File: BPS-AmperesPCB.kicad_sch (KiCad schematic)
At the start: 44 parts, among them J1 Conn_01x04, J2 PeripheralCANConnector, J3 PeripheralCANConnector, U1 PeripheralSOM, U2 INA145UA/2K5, U3 AMC1300BDWV, U4 RO-123.3S_HP

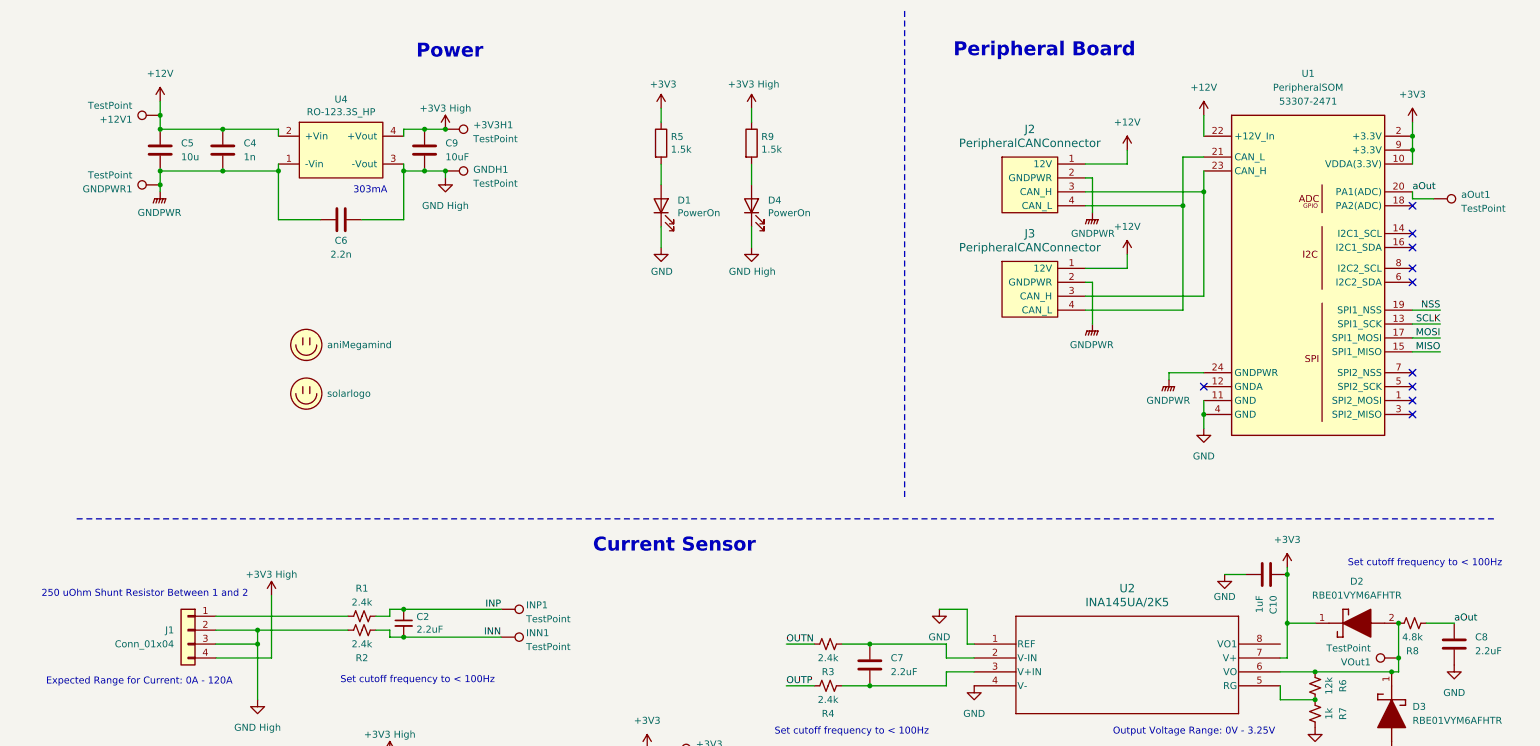
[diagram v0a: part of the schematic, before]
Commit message: initial sch change, added PSOM components
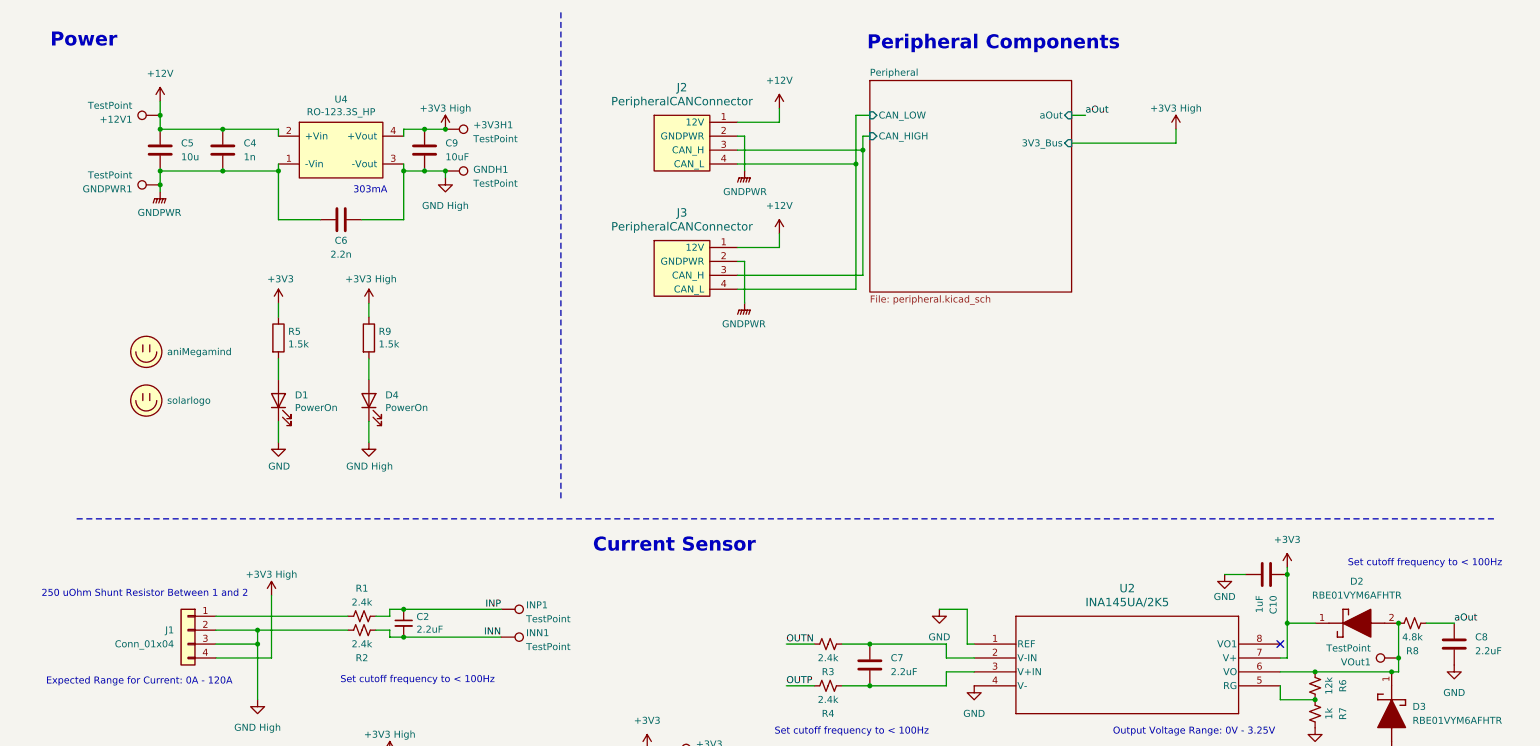
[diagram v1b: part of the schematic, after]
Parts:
- removed U1: PeripheralSOM, UTSVT_Special:PeripheralSOM, symbol utsvt-misc:PeripheralSOM
- removed aOut1: TestPoint, TestPoint:TestPoint_Keystone_5005-5009_Compact, symbol Connector:TestPoint
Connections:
- net Peripheral/CAN_HIGH: now reaches J2.3 (CAN_H), J3.3 (CAN_H)
- net Peripheral/CAN_LOW: now reaches J2.4 (CAN_L), J3.4 (CAN_L)
- no-connect marks 10 -> 1
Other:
- added sheet Peripheral (peripheral.kicad_sch)
- note added: "Peripheral Components"
- note removed: "Peripheral Board"
- moved on the sheet: D1, D4, R5, R9

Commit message: migrated to KiCad 9
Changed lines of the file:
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@@
 (kicad_sch
-	(version 20231120)
+	(version 20250114)
 	(generator "eeschema")
-	(generator_version "8.0")
+	(generator_version "9.0")
 	(paper "A4")
+	(text "Maximum Voltage Protected: -2.7V - 6V"
+		(exclude_from_sim no)
+		(at 261.366 158.75 0)
+		(effects
+			(font
+				(size 1.27 1.27)
+			)
+		)
+	)
+	(text "Output Voltage Range: 0V - 3.25V"
+		(exclude_from_sim no)
+		(at 225.552 145.542 0)
+		(effects
+			(font
+				(size 1.27 1.27)
+			)
+		)
+	)
+	(text "Total Gain (V/A): 0.027"
+		(exclude_from_sim no)
+		(at 182.626 158.496 0)
+		(effects
+			(font
+				(size 1.27 1.27)
+			)
+		)
+	)
+	(text "Output Voltage Range: 0V - 0.25V"
+		(exclude_from_sim no)
+		(at 124.968 172.466 0)
+		(effects
+			(font
+				(size 1.27 1.27)
+			)
+		)
+	)
+	(text "Peripheral Components"
+		(exclude_from_sim no)
+		(at 165.862 21.336 0)
+		(effects
+			(font
+				(size 2.54 2.54)
+				(thickness 0.508)
+				(bold yes)
+			)
+			(justify left bottom)
+		)
+	)
+	(text "Set cutoff frequency to < 100Hz"
+		(exclude_from_sim no)
+		(at 83.82 136.144 0)
+		(effects
+			(font
+				(size 1.27 1.27)
+			)
+		)
+	)
+	(text "Set cutoff frequency to < 100Hz"
+		(exclude_from_sim no)
+		(at 163.068 145.542 0)
+		(effects
+			(font
+				(size 1.27 1.27)
+			)
+		)
+	)
+	(text "303mA"
+		(exclude_from_sim no)
+		(at 75.184 46.736 0)
+		(effects
+			(font
+				(size 1.27 1.27)
+			)
+		)
+	)
+	(text "Input Voltage Range: 0V - 0.03V"
+		(exclude_from_sim no)
+		(at 57.15 160.274 0)
+		(effects
+			(font
+				(size 1.27 1.27)
+			)
+		)
+	)
+	(text "Set cutoff frequency to < 100Hz"
+		(exclude_from_sim no)
+		(at 267.716 114.808 0)
+		(effects
+			(font
+				(size 1.27 1.27)
+			)
+		)
+	)
+	(text "Current Sensor"
+		(exclude_from_sim no)
+		(at 115.824 113.03 0)
+		(effects
+			(font
+				(size 2.54 2.54)
+				(thickness 0.508)
+				(bold yes)
+			)
+			(justify left bottom)
+		)
+	)
+	(text "Power"
+		(exclude_from_sim no)
+		(at 16.764 20.828 0)
+		(effects
+			(font
+				(size 2.54 2.54)
+				(thickness 0.508)
+				(bold yes)
+			)
+			(justify left bottom)
+		)
+	)
+	(text "Expected Range for Current: 0A - 120A"
+		(exclude_from_sim no)
+		(at 33.02 136.398 0)
+		(effects
+			(font
+				(size 1.27 1.27)
+			)
+		)
+	)
+	(text "250 uOhm Shunt Resistor Between 1 and 2\n"
+		(exclude_from_sim no)
+		(at 34.036 120.396 0)
+		(effects
+			(font
+				(size 1.27 1.27)
+			)
+		)
+	)
+	(text "Max Protected Current: 222A"
+		(exclude_from_sim no)
+		(at 184.658 162.306 0)
+		(effects
+			(font
+				(size 1.27 1.27)
+			)
+		)
+	)
 	(junction
 		(at 85.09 35.56)
@@
 		)
 	)
-	(text "Maximum Voltage Protected: -2.7V - 6V"
-		(exclude_from_sim no)
-		(at 261.366 158.75 0)
-		(effects
-			(font
-				(size 1.27 1.27)
-			)
-		)
-	)
-	(text "Output Voltage Range: 0V - 3.25V"
-		(exclude_from_sim no)
-		(at 225.552 145.542 0)
-		(effects
-			(font
-				(size 1.27 1.27)
-			)
-		)
-	)
-	(text "Total Gain (V/A): 0.027"
-		(exclude_from_sim no)
-		(at 182.626 158.496 0)
-		(effects
-			(font
-				(size 1.27 1.27)
-			)
-		)
-	)
-	(text "Output Voltage Range: 0V - 0.25V"
-		(exclude_from_sim no)
-		(at 124.968 172.466 0)
-		(effects
-			(font
-				(size 1.27 1.27)
-			)
-		)
-	)
-	(text "Peripheral Components"
-		(exclude_from_sim no)
-		(at 165.862 21.336 0)
-		(effects
-			(font
-				(size 2.54 2.54)
-				(thickness 0.508)
-				(bold yes)
-			)
-			(justify left bottom)
-		)
-	)
-	(text "Set cutoff frequency to < 100Hz"
-		(exclude_from_sim no)
-		(at 83.82 136.144 0)
-		(effects
-			(font
-				(size 1.27 1.27)
-			)
-		)
-	)
-	(text "Set cutoff frequency to < 100Hz"
-		(exclude_from_sim no)
-		(at 163.068 145.542 0)
-		(effects
-			(font
-				(size 1.27 1.27)
-			)
-		)
-	)
-	(text "303mA"
-		(exclude_from_sim no)
-		(at 75.184 46.736 0)
-		(effects
-			(font
-				(size 1.27 1.27)
-			)
-		)
-	)
-	(text "Input Voltage Range: 0V - 0.03V"
-		(exclude_from_sim no)
-		(at 57.15 160.274 0)
-		(effects
-			(font
-				(size 1.27 1.27)
-			)
-		)
-	)
-	(text "Set cutoff frequency to < 100Hz"
-		(exclude_from_sim no)
-		(at 267.716 114.808 0)
-		(effects
-			(font
-				(size 1.27 1.27)
-			)
-		)
-	)
-	(text "Current Sensor"
-		(exclude_from_sim no)
-		(at 115.824 113.03 0)
-		(effects
-			(font
-				(size 2.54 2.54)
-				(thickness 0.508)
-				(bold yes)
-			)
-			(justify left bottom)
-		)
-	)
-	(text "Power"
-		(exclude_from_sim no)
-		(at 16.764 20.828 0)
-		(effects
-			(font
-				(size 2.54 2.54)
-				(thickness 0.508)
-				(bold yes)
-			)
-			(justify left bottom)
-		)
-	)
-	(text "Expected Range for Current: 0A - 120A"
-		(exclude_from_sim no)
-		(at 33.02 136.398 0)
-		(effects
-			(font
-				(size 1.27 1.27)
-			)
-		)
-	)
-	(text "250 uOhm Shunt Resistor Between 1 and 2\n"
-		(exclude_from_sim no)
-		(at 34.036 120.396 0)
-		(effects
-			(font
-				(size 1.27 1.27)
-			)
-		)
-	)
-	(text "Max Protected Current: 222A"
-		(exclude_from_sim no)
-		(at 184.658 162.306 0)
-		(effects
-			(font
-				(size 1.27 1.27)
-			)
-		)
-	)
 	(label "INP"
 		(at 99.06 123.19 180)
@@
 		(at 166.37 26.67)
 		(size 36.83 38.608)
+		(exclude_from_sim no)
+		(in_bom yes)
+		(on_board yes)
+		(dnp no)
 		(fields_autoplaced yes)
 		(stroke
@@
 		)
 	)
+	(embedded_fonts no)
 )

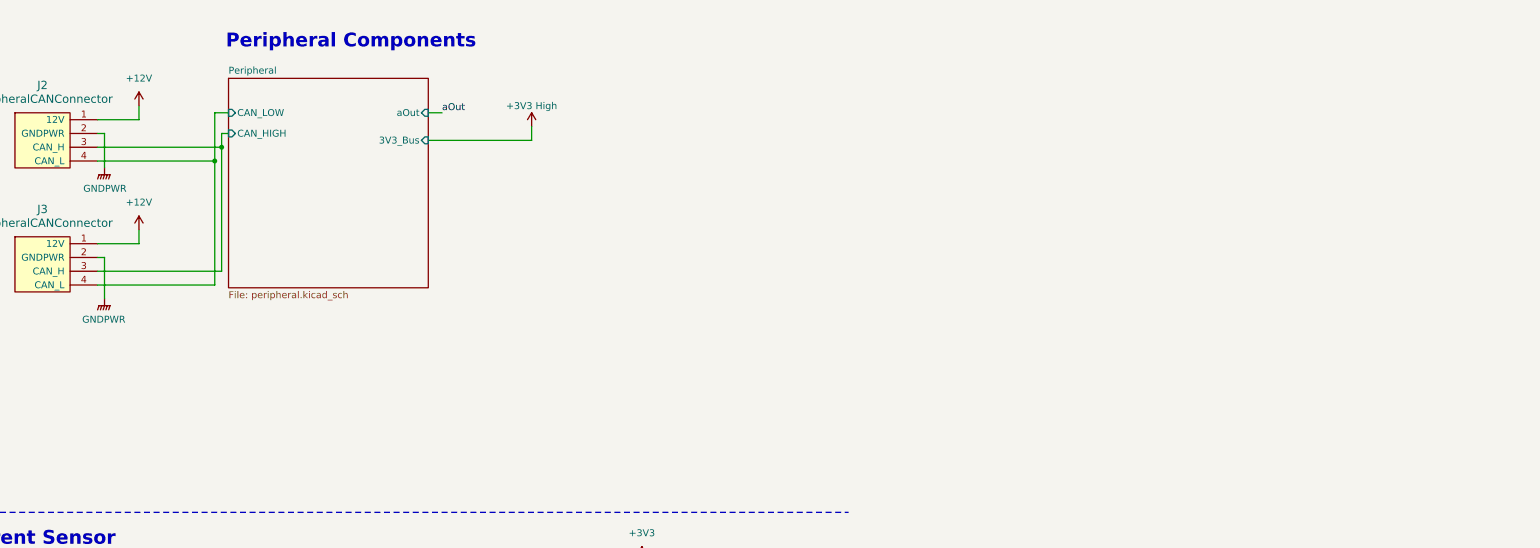
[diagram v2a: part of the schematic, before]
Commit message: replaced UTSVT with KiCAD-Bild submodule
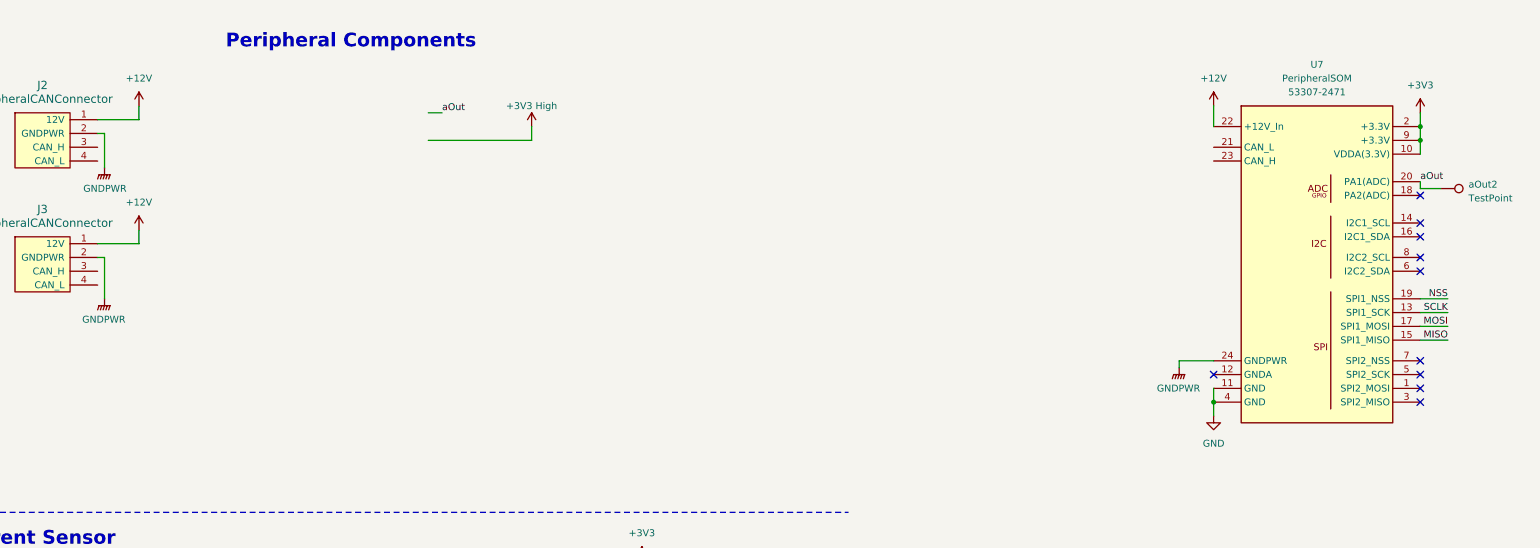
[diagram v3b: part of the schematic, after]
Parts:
- added U7: PeripheralSOM, UTSVT_Special:PeripheralSOM, symbol utsvt-misc:PeripheralSOM
- added aOut2: TestPoint, TestPoint:TestPoint_Keystone_5005-5009_Compact, symbol Connector:TestPoint
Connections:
- net +12V: now also U7.22 (+12V_In)
- net +3V3: now also U7.10 (VDDA(3.3V)), U7.2 (+3.3V), U7.9 (+3.3V)
- net GND: now also U7.11 (GND), U7.4 (GND)
- net GNDPWR: now also U7.24 (GNDPWR)
- net aOut: now also U7.20 (PA1(ADC)), aOut2.1
- net Peripheral/CAN_HIGH: no longer names the net of J2.3 (CAN_H)
- net Peripheral/CAN_HIGH: no longer J3.3 (CAN_H)
- net Peripheral/CAN_LOW: no longer names the net of J2.4 (CAN_L)
- net Peripheral/CAN_LOW: no longer J3.4 (CAN_L)
- new net MISO: U7.15 (SPI1_MISO)
- new net MOSI: U7.17 (SPI1_MOSI)
- new net NSS: U7.19 (SPI1_NSS)
- new net SCLK: U7.13 (SPI1_SCK)
- no-connect marks 1 -> 11
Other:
- removed sheet Peripheral

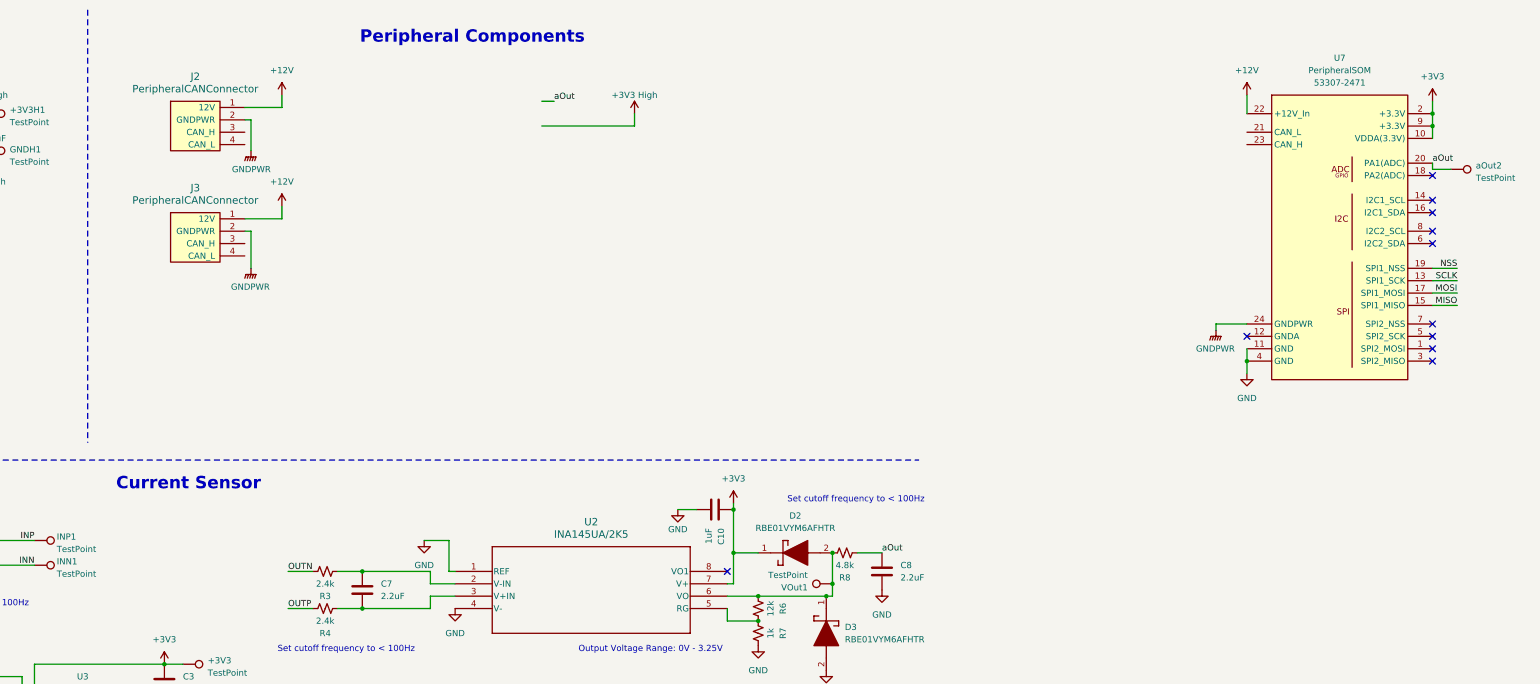
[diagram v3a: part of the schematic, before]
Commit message: mcu and CAN added, missing Amperes DC-DC sym / footprint
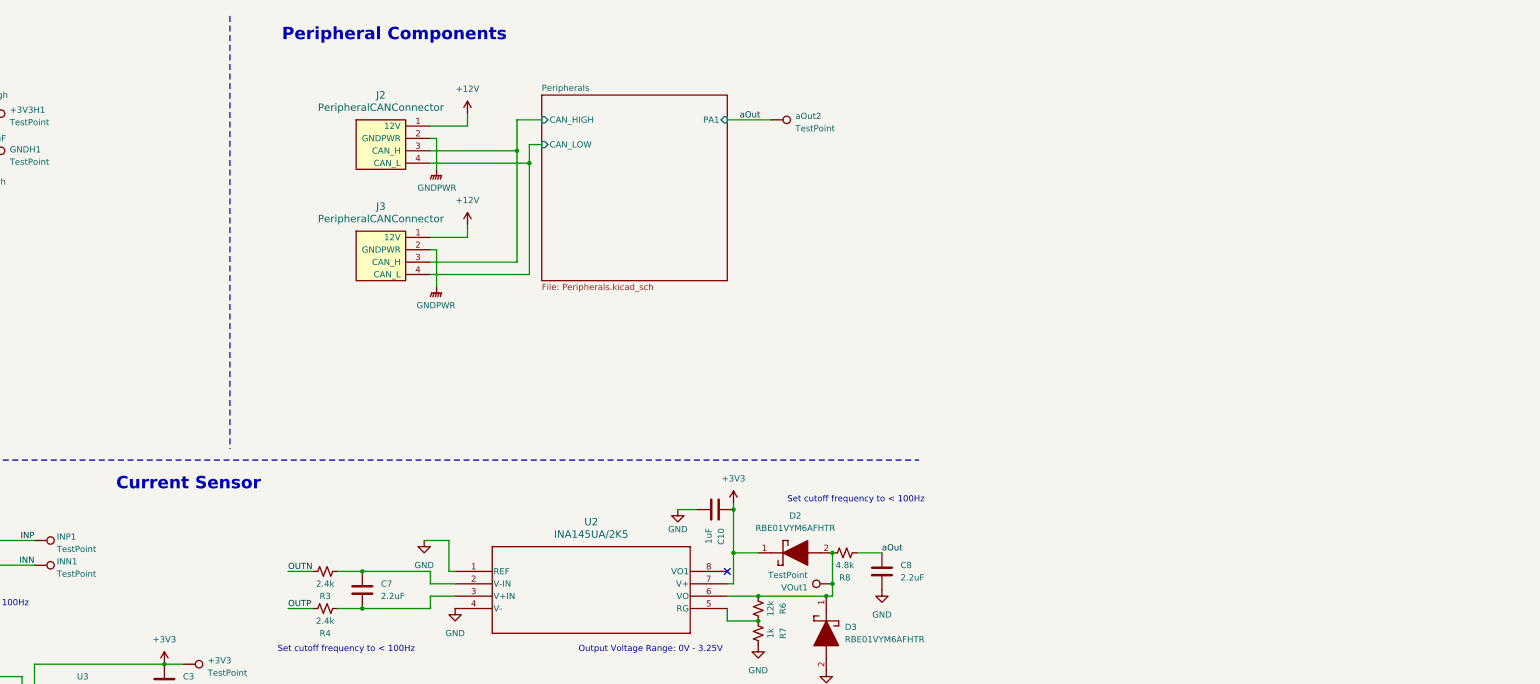
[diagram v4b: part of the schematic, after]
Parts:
- removed D2, D3: RBE01VYM6AFHTR, Parts:RBE01VYM6AFHTR, symbol usvt-chips:RBE01VYM6AFHTR
- removed U2: INA145UA/2K5, Parts:D8, symbol usvt-chips:INA145UA_2K5
- removed U7: PeripheralSOM, UTSVT_Special:PeripheralSOM, symbol utsvt-misc:PeripheralSOM
- added D2, D3: RBE01VYM6AFHTR, Parts:RBE01VYM6AFHTR, symbol RBE01:RBE01VYM6AFHTR
- added U2: INA145UA/2K5, Parts:D8, symbol INA145:INA145UA_2K5
- LOGO1: footprint Parts:aniMegamind -> UTSVT_Logos:Hallock_Image_Small
- LOGO2: footprint UTSVT_Special:UTSVT_Logo_Symbol -> UTSVT_Logos:Hallock_Image_Small
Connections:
- net +3V3: now also D2.1 (K), U2.7 (V+)
- net GND: now also D3.2 (A), U2.1 (REF), U2.4 (V-)
- net at C7.1, R3.1: now also U2.2 (V-IN)
- net at C7.2, R4.1: now also U2.3 (V+IN)
- net at R6.2, R7.1: now also U2.5 (RG)
- net at R6.1, R8.2, VOut1.1: now also D2.2 (A), D3.1 (K), U2.6 (VO)
- net Peripherals/CAN_HIGH: now reaches J2.3 (CAN_H)
- net Peripherals/CAN_HIGH: now also J3.3 (CAN_H)
- net Peripherals/CAN_LOW: now reaches J2.4 (CAN_L)
- net Peripherals/CAN_LOW: now also J3.4 (CAN_L)
- no-connect marks 11 -> 1
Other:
- added sheet Peripherals (Peripherals.kicad_sch)
- moved on the sheet: aOut2

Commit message: isolated 3v3 done?
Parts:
- removed C6: 2.2n, Capacitor_SMD:C_0805_2012Metric, symbol Device:C
- removed C9: 10uF, Capacitor_SMD:C_0805_2012Metric, symbol Device:C
- removed D1: PowerOn, LED_SMD:LED_0805_2012Metric, symbol Device:LED
- removed R5: 1.5k, Resistor_SMD:R_0805_2012Metric, symbol Device:R
- removed U4: RO-123.3S_HP, UTSVT_ICs:RI3_DC_Converter, symbol utsvt-power-regulators:RO-123.3S_HP
- added D5, D6: PowerOn, LED_SMD:LED_0805_2012Metric, symbol Device:LED
- added IC1: 1769205241, 1769205241, symbol WE_1769205241:1769205241
- added IC2: TLV70130DBVR, UTSVT_Power:TLV70130DBVR, symbol utsvt-power:TLV70130DBVR
- added R10, R11: 1.5k, Resistor_SMD:R_0805_2012Metric, symbol Device:R
- C4: value 1n -> 100nF; footprint Capacitor_SMD:C_0805_2012Metric -> (none)
- C5: value 10u -> 100nF; footprint Capacitor_SMD:C_0805_2012Metric -> (none)
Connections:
- net +12V: now also IC1.2 (+VIN); no longer C4.1, C5.1
- net +3V3: now also R11.1
- net +3V3 High: now also C5.1, IC2.1 (OUT), R10.1; no longer R9.1
- net GND: now also D6.1 (K)
- net GND High: now also C4.2, C5.2, D5.1 (K), IC1.4 (-VOUT), IC2.2 (GND)
- net GNDPWR: now also IC1.1 (-VIN); no longer C4.2, C5.2
- new net: D5.2 (A), R10.2
- new net: D6.2 (A), R11.2
- new net +5V: C4.1, IC1.5 (+VOUT), IC2.3 (IN), R9.1
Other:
- note added: "12V -> 5V DC-DC Converter"
- note added: "5V -> 3.3V LDO"
- note added: "Isolated 3.3 V"
- note added: "Non-Isolated 3.3 V"
- note removed: "303mA"
- moved on the sheet: +12V1, +3V3, +3V3H1, C1, C10, C2, C3, C7, C8, D2, D3, D4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
